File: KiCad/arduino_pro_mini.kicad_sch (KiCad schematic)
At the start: 6 parts, among them IC101 ATMEGA328P-AU, IC102 UA78M05CDCYR, Y401 16Mhz

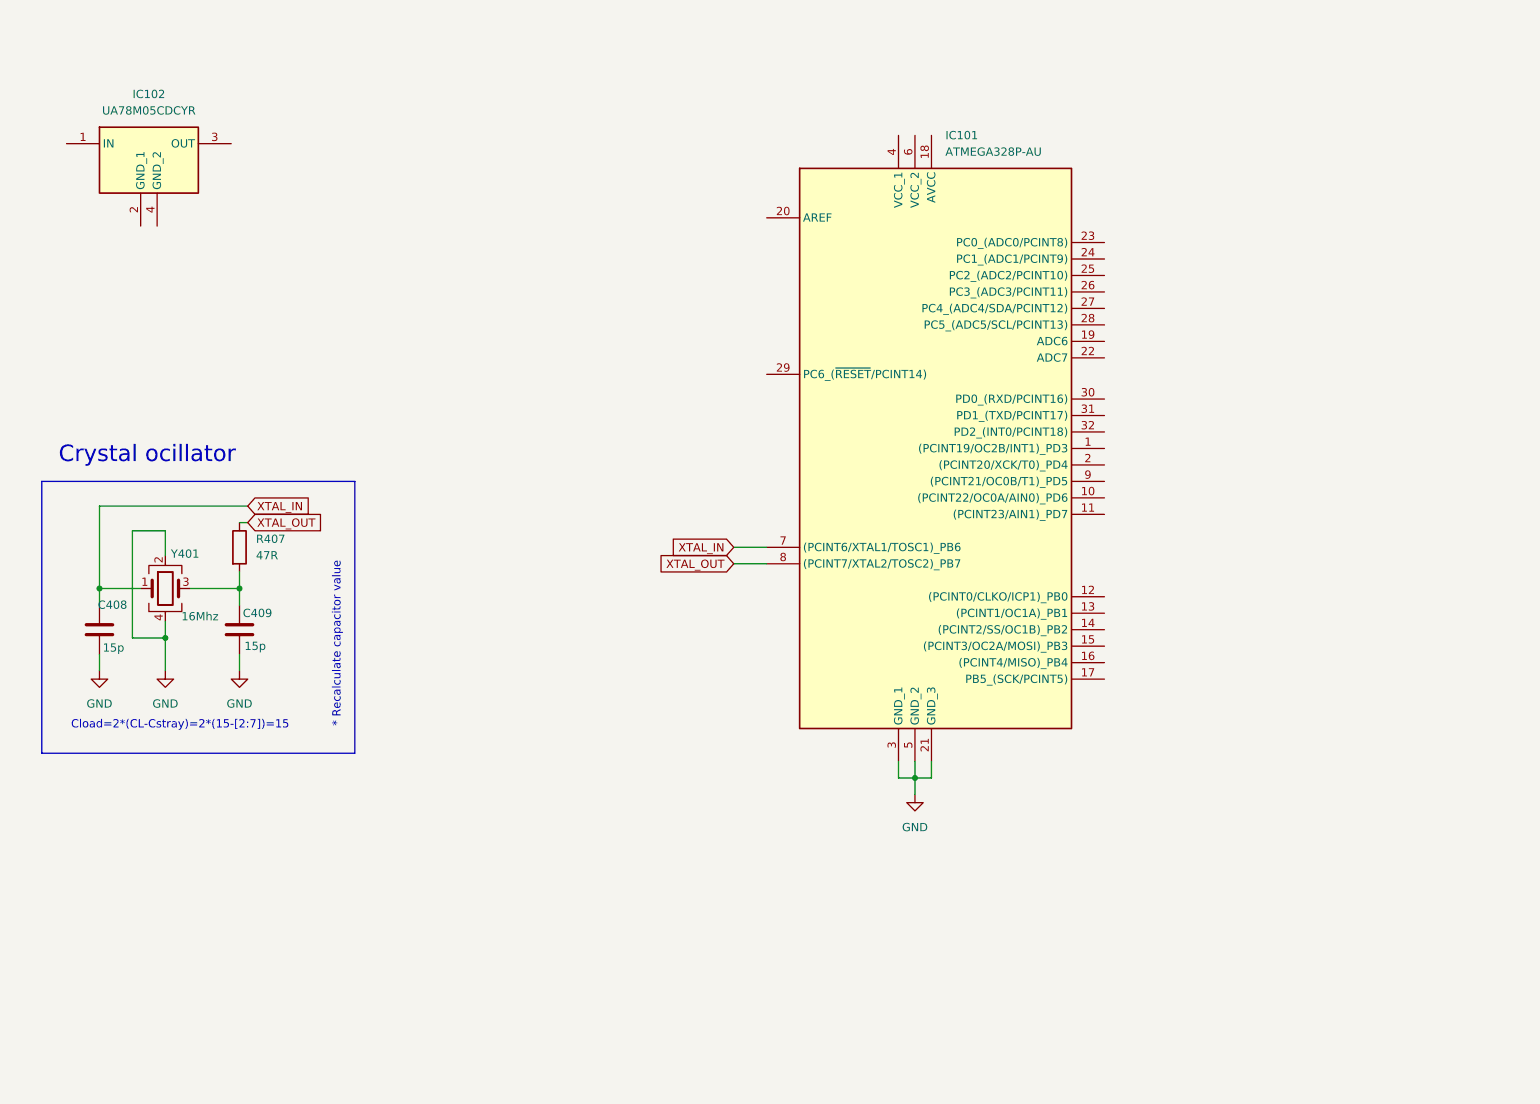
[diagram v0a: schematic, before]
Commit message: Add pushbutton
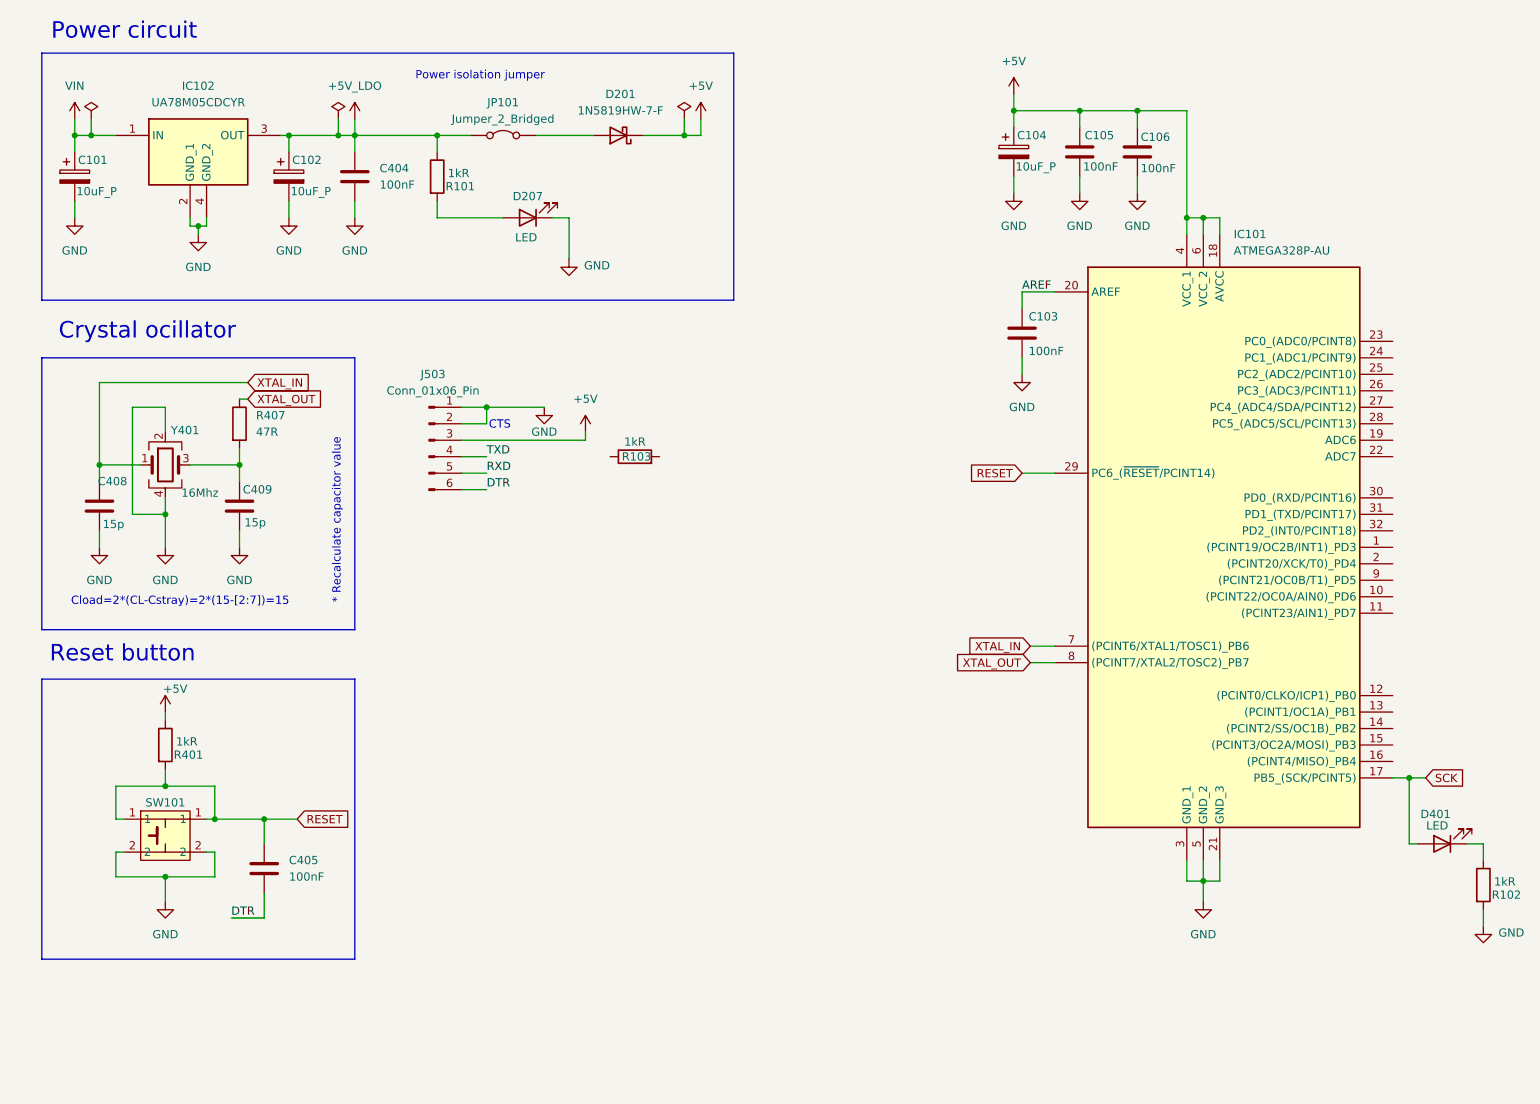
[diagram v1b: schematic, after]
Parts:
- added C101, C102, C104: 10uF_P, Capacitor_Tantalum_SMD:CP_EIA-3216-18_Kemet-A, symbol Device:C_Polarized
- added C103, C105, C106, C404, C405: 100nF, Capacitor_SMD:C_0402_1005Metric, symbol Device:C
- added D201: 1N5819HW-7-F, Diode_SMD:D_SOD-123, symbol Device:D_Schottky
- added D207, D401: LED, LED_SMD:LED_0603_1608Metric, symbol Device:LED
- added J503: Conn_01x06_Pin, Connector_PinHeader_2.54mm:PinHeader_1x06_P2.54mm_Vertical, symbol Connector:Conn_01x06_Pin
- added JP101: Jumper_2_Bridged, TestPoint:TestPoint_2Pads_Pitch2.54mm_Drill0.8mm, symbol Jumper:Jumper_2_Bridged
- added R101, R102, R103, R401: 1kR, Resistor_SMD:R_0805_2012Metric, symbol Device:R
- added SW101: ~, atmega328p:SW_PUSH_6mm_H5mm, symbol atmega328p:SW_PUSH_6mm_H5mm
- C408, C409: DigiKey Part Number 490-11191-6-ND -> (none)
- IC102: Manufacturer_Name Texas Instruments -> (none); Manufacturer_Part_Number UA78M05CDCYR -> (none); Mouser Part Number 595-UA78M05CDCYR -> (none); Mouser Price/Stock https://www.mouser.co.uk/ProductDetail/Texas-Instruments/UA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 -> (none)
- R407: DigiKey Part Number P47JDKR-ND -> (none)
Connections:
- net GND: now also IC102.2 (GND_1), IC102.4 (GND_2), C101.2, C102.2, C103.2, C104.2, C105.2, C106.2, C404.2, D207.1 (K), J503.1 (Pin_1), J503.2 (Pin_2), R102.2, SW101.2
- net VIN: now reaches IC102.1 (IN)
- net VIN: now also C101.1
- net +5V_LDO: now reaches IC102.3 (OUT)
- net +5V_LDO: now also C102.1, C404.1, JP101.1 (A), R101.1
- net SCK: now reaches IC101.17 (PB5_(SCK/PCINT5))
- net SCK: now also D401.2 (A)
- net +5V: now reaches IC101.18 (AVCC)
- net +5V: now also IC101.4 (VCC_1), IC101.6 (VCC_2), C104.1, C105.1, C106.1, D201.1 (K), J503.3 (Pin_3), R401.1
- net AREF: now reaches IC101.20 (AREF)
- net AREF: now also C103.1
- net RESET: now reaches IC101.29 (PC6_(~{RESET}/PCINT14))
- net RESET: now also C405.1, R401.2, SW101.1
- new net: D207.2 (A), R101.2
- new net: D401.1 (K), R102.1
- new net: D201.2 (A), JP101.2 (B)
- new net DTR: C405.2, J503.6 (Pin_6)
- new net RXD: J503.5 (Pin_5)
- new net TXD: J503.4 (Pin_4)
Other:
- note added: "CTS"
- note added: "Power circuit"
- note added: "Power isolation jumper"
- note added: "Reset button"
- moved on the sheet: C408, C409, IC101, IC102, R407, Y401

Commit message: Initial scheme
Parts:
- added J102, J103: Conn_01x15_Pin, Connector_PinHeader_2.54mm:PinHeader_1x15_P2.54mm_Vertical, symbol Connector:Conn_01x15_Pin
- added J104: Conn_02x03_Odd_Even, Connector_PinHeader_2.54mm:PinHeader_2x03_P2.54mm_Vertical, symbol Connector_Generic:Conn_02x03_Odd_Even
- added R104: 1kR, Resistor_SMD:R_0805_2012Metric, symbol Device:R
- renumbered C104 to C101, C105 to C102, C106 to C103, C101 to C104, C102 to C105, C404 to C106, C103 to C107, C408 to C108, C409 to C109, C405 to C110, D201 to D101, D207 to D102, D401 to D103, IC102 to IC101, IC101 to IC102, J503 to J101, R407 to R102, R401 to R105, R102 to R106, Y401 to Y101
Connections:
- net +5V: now also J103.4 (Pin_4), J104.2 (Pin_2)
- net AREF: now also J103.13 (Pin_13)
- net GND: now also J102.4 (Pin_4), J103.14 (Pin_14), J103.2 (Pin_2), J104.6 (Pin_6)
- net RESET: now also J102.3 (Pin_3), J103.3 (Pin_3), J104.5 (Pin_5)
- net RXD: now also R104.1
- net TXD: now also R103.1
- net VIN: now also J103.1 (Pin_1)
- net D0_RX: now reaches R103.2
- net D0_RX: now also IC102.30 (PD0_(RXD/PCINT16)), J102.2 (Pin_2)
- net D3: now reaches IC102.1 ((PCINT19/OC2B/INT1)_PD3)
- net D3: now also J102.6 (Pin_6)
- net D6: now reaches IC102.10 ((PCINT22/OC0A/AIN0)_PD6)
- net D6: now also J102.9 (Pin_9)
- net D7: now reaches IC102.11 ((PCINT23/AIN1)_PD7)
- net D7: now also J102.10 (Pin_10)
- net D8: now reaches IC102.12 ((PCINT0/CLKO/ICP1)_PB0)
- net D8: now also J102.11 (Pin_11)
- net D9: now reaches IC102.13 ((PCINT1/OC1A)_PB1)
- net D9: now also J102.12 (Pin_12)
- net D10: now reaches IC102.14 ((PCINT2/SS/OC1B)_PB2)
- net D10: now also J102.13 (Pin_13)
- net D11_MOSI: now reaches IC102.15 ((PCINT3/OC2A/MOSI)_PB3)
- net D11_MOSI: now also J102.14 (Pin_14), J104.4 (Pin_4)
- net D12_MISO: now reaches IC102.16 ((PCINT4/MISO)_PB4)
- net D12_MISO: now also J102.15 (Pin_15), J104.1 (Pin_1)
- net A6: now reaches IC102.19 (ADC6)
- net A6: now also J103.6 (Pin_6)
- net D4: now reaches IC102.2 ((PCINT20/XCK/T0)_PD4)
- net D4: now also J102.7 (Pin_7)
- net A7: now reaches IC102.22 (ADC7)
- net A7: now also J103.5 (Pin_5)
- net A0: now reaches IC102.23 (PC0_(ADC0/PCINT8))
- net A0: now also J103.12 (Pin_12)
- net A1: now reaches IC102.24 (PC1_(ADC1/PCINT9))
- net A1: now also J103.11 (Pin_11)
- net A2: now reaches IC102.25 (PC2_(ADC2/PCINT10))
- net A2: now also J103.10 (Pin_10)
- net A3: now reaches IC102.26 (PC3_(ADC3/PCINT11))
- net A3: now also J103.9 (Pin_9)
- net A4: now reaches IC102.27 (PC4_(ADC4/SDA/PCINT12))
- net A4: now also J103.8 (Pin_8)
- net A5: now reaches IC102.28 (PC5_(ADC5/SCL/PCINT13))
- net A5: now also J103.7 (Pin_7)
- net D1_TX: now reaches IC102.31 (PD1_(TXD/PCINT17))
- net D1_TX: now also J102.1 (Pin_1), R104.2
- net D2: now reaches IC102.32 (PD2_(INT0/PCINT18))
- net D2: now also J102.5 (Pin_5)
- net D5: now reaches IC102.9 ((PCINT21/OC0B/T1)_PD5)
- net D5: now also J102.8 (Pin_8)
- net SCK renamed D13_SCK
- net D13_SCK: now also J103.15 (Pin_15), J104.3 (Pin_3)
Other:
- note added: "ICSP pin header"
- note added: "Left/Right pin header"
- note added: "Need to swap TX and RX signals"
- note added: "UART connector"

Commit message: first pcb component placement
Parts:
- removed C106: 100nF, Capacitor_SMD:C_0402_1005Metric, symbol Device:C
- removed R102: 47R, Resistor_SMD:R_0402_1005Metric, symbol Device:R
- removed SW101: ~, atmega328p:SW_PUSH_6mm_H5mm, symbol atmega328p:SW_PUSH_6mm_H5mm
- added SW101: SW_Omron_B3FS, Button_Switch_SMD:SW_SPST_Omron_B3FS-100xP, symbol Switch:SW_Omron_B3FS
- R101: footprint Resistor_SMD:R_0805_2012Metric -> Resistor_SMD:R_0402_1005Metric
- R102: renamed from R103; footprint Resistor_SMD:R_0805_2012Metric -> Resistor_SMD:R_0402_1005Metric
- R103: renamed from R104; footprint Resistor_SMD:R_0805_2012Metric -> Resistor_SMD:R_0402_1005Metric
- R104: renamed from R105; footprint Resistor_SMD:R_0805_2012Metric -> Resistor_SMD:R_0402_1005Metric
- R105: renamed from R106; footprint Resistor_SMD:R_0805_2012Metric -> Resistor_SMD:R_0402_1005Metric
- renumbered C107 to C106, C108 to C107, C109 to C108, C110 to C109
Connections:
- net GND: now also SW101.1
- net RESET: now also SW101.2
- net XTAL_OUT: now also C108.1, Y101.3
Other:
- moved on the sheet: D101, D102, JP101, R101, R104

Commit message: Add signal traces to PCB
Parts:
- added C104: 100nF, Capacitor_SMD:C_0805_2012Metric, symbol Device:C
- C102, C103: footprint Capacitor_SMD:C_0402_1005Metric -> Capacitor_SMD:C_0805_2012Metric
- C107: renamed from C106; footprint Capacitor_SMD:C_0402_1005Metric -> Capacitor_SMD:C_0805_2012Metric
- C110: renamed from C109; footprint Capacitor_SMD:C_0402_1005Metric -> Capacitor_SMD:C_0805_2012Metric
- R101, R102, R103, R104, R105: footprint Resistor_SMD:R_0402_1005Metric -> Resistor_SMD:R_0603_1608Metric
- renumbered C104 to C105, C105 to C106, C107 to C108, C108 to C109
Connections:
- net +5V: now also C104.1
- net D0_RX: now also J102.1 (Pin_1); no longer J102.2 (Pin_2)
- net D1_TX: now also J102.2 (Pin_2); no longer J102.1 (Pin_1)
- net GND: now also C104.2
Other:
- moved on the sheet: C101, C102, C103

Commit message: All connected
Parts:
- C108, C109: footprint Capacitor_SMD:C_0402_1005Metric -> Capacitor_SMD:C_0603_1608Metric
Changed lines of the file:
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@@
 			)
 		)
-		(property "Footprint" "Capacitor_SMD:C_0402_1005Metric"
+		(property "Footprint" "Capacitor_SMD:C_0603_1608Metric"
 			(at 26.3652 93.98 0)
 			(effects
@@
 			)
 		)
-		(property "Footprint" "Capacitor_SMD:C_0402_1005Metric"
+		(property "Footprint" "Capacitor_SMD:C_0603_1608Metric"
 			(at 47.9552 93.98 0)
 			(effects

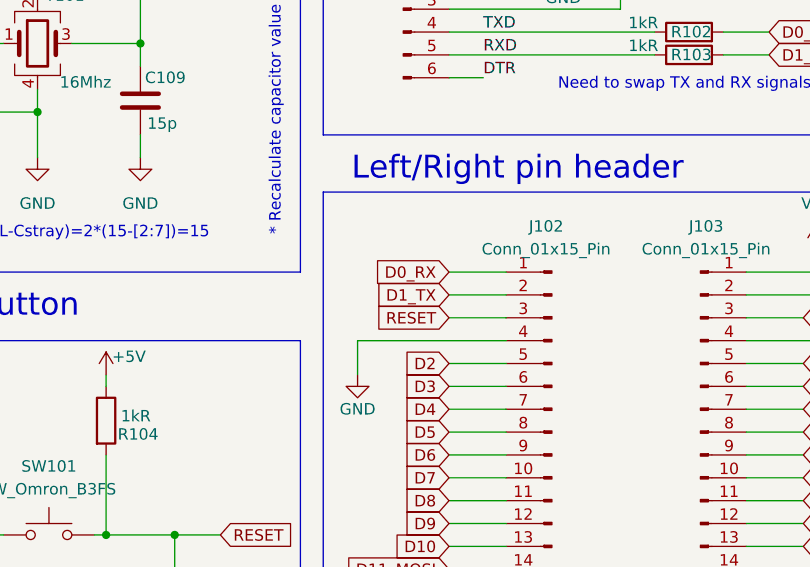
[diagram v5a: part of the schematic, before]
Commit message: silk screen updates
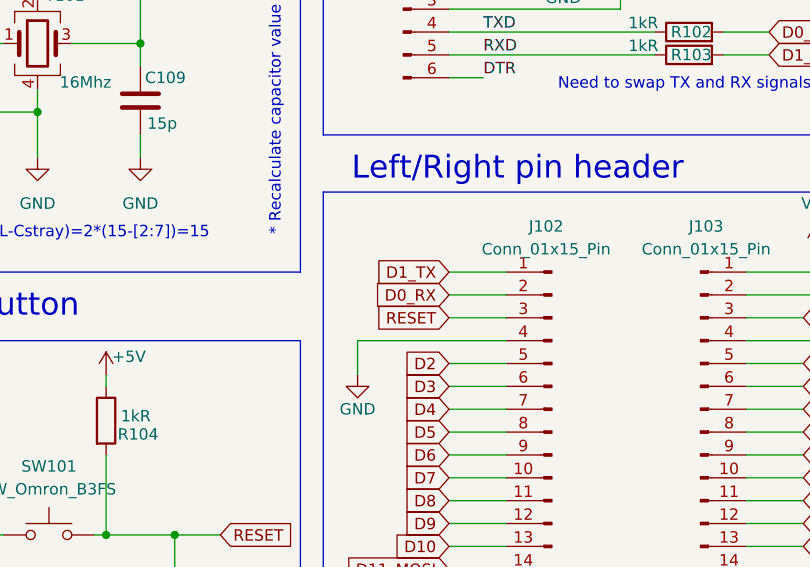
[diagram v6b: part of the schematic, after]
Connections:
- net D0_RX: now also J102.2 (Pin_2); no longer J102.1 (Pin_1)
- net D1_TX: now also J102.1 (Pin_1); no longer J102.2 (Pin_2)
